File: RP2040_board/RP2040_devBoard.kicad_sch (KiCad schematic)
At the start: 27 parts, among them J1 USB_B_Micro, SW1 SW_Push, U1 RP2040, U2 AMS1117, U3 W25Q128JVS, Y1 Crystal

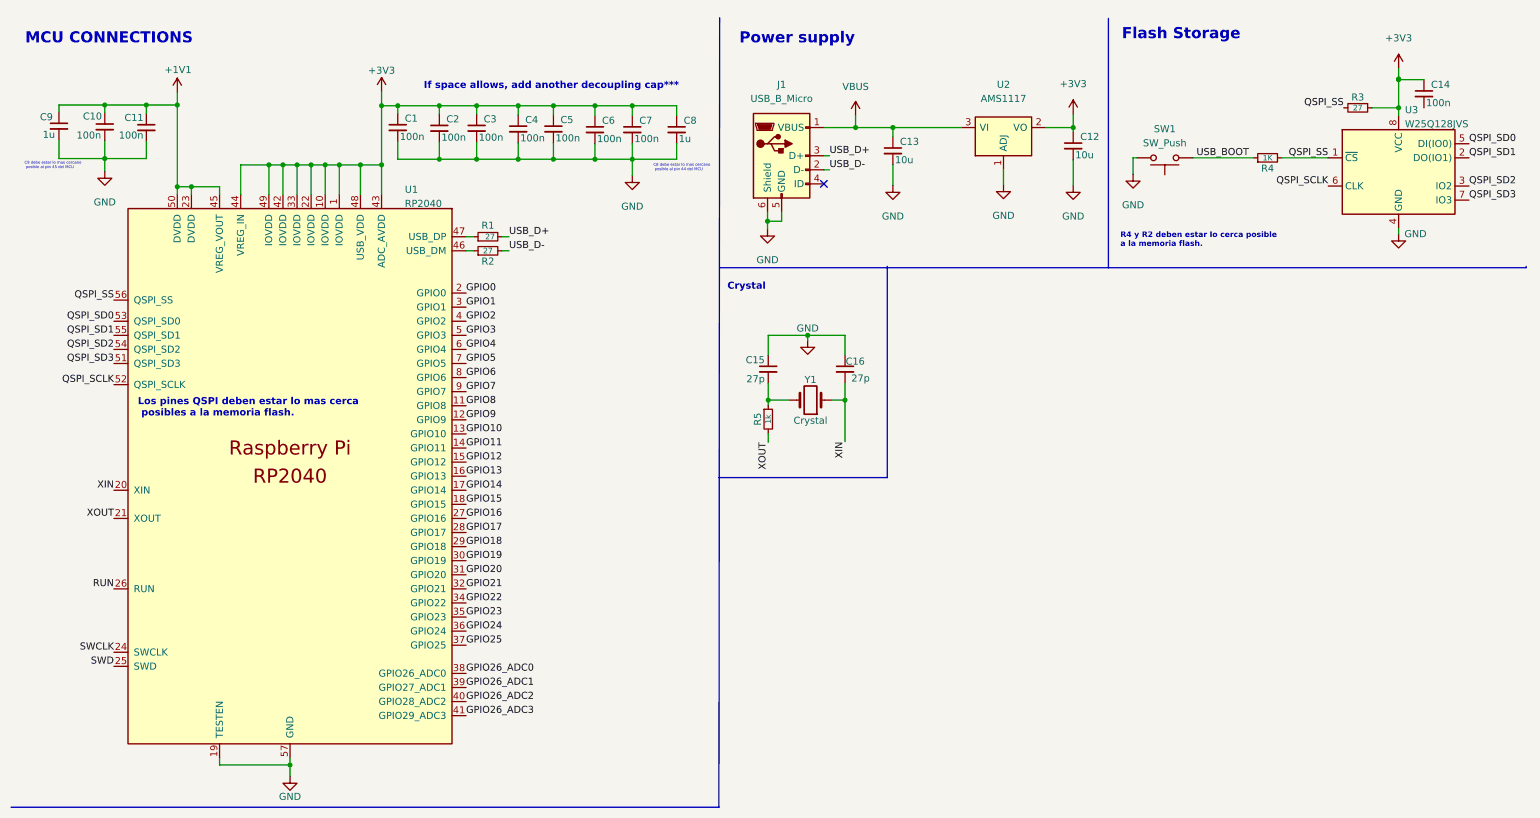
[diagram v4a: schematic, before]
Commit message: SCH: finishe with the crystal and added the pin headers
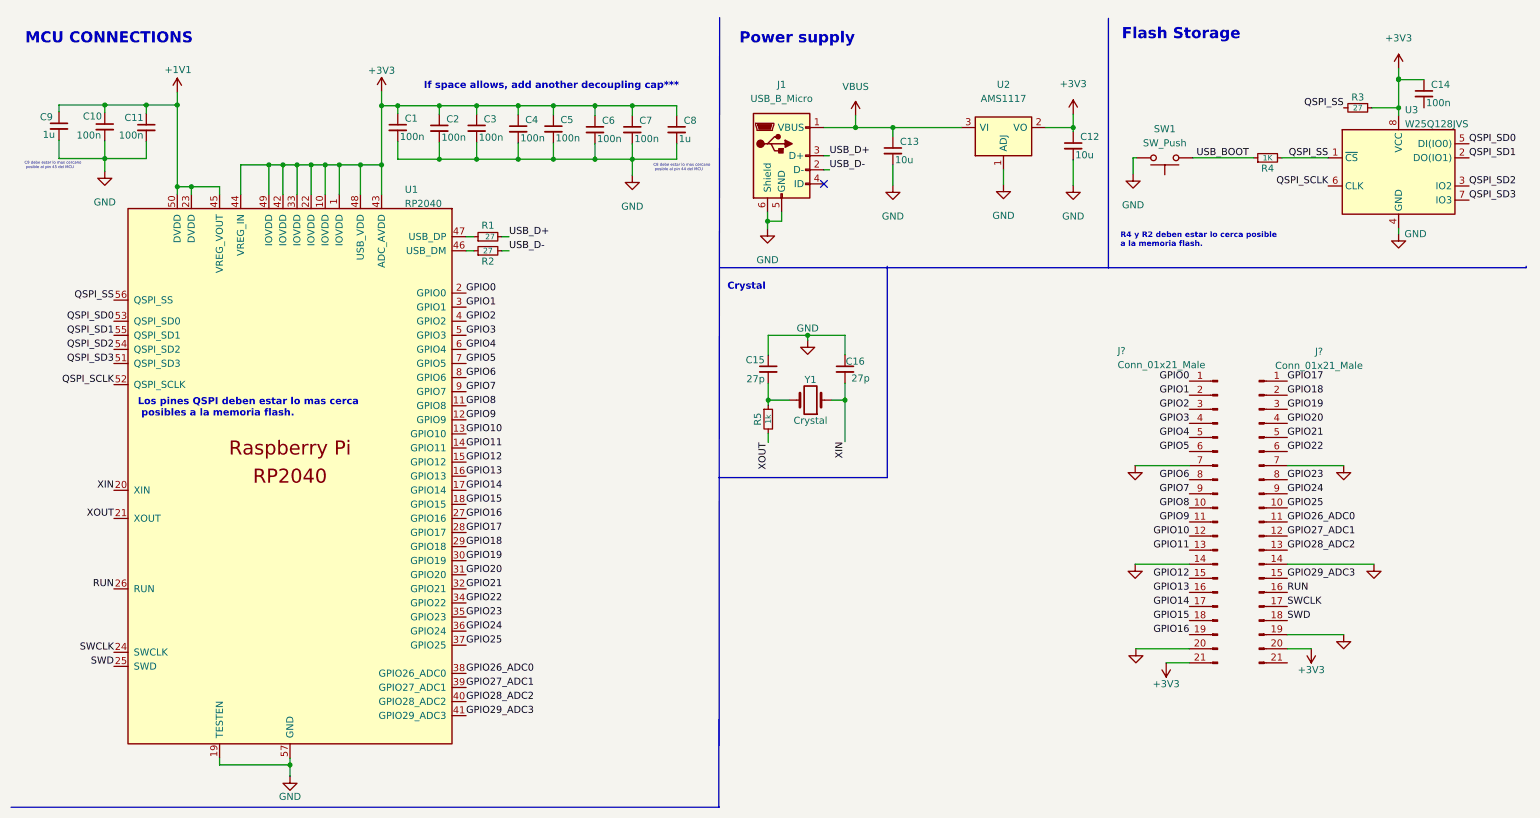
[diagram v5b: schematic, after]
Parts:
- added J? (x2): Conn_01x21_Male, symbol Connector:Conn_01x21_Male
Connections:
- net +3V3: now also J?.20 (Pin_20), J?.21 (Pin_21)
- net GND: now also J?.14 (Pin_14), J?.14 (Pin_14), J?.19 (Pin_19), J?.20 (Pin_20), J?.7 (Pin_7), J?.7 (Pin_7)
- net GPIO0: now also J?.1 (Pin_1)
- net GPIO1: now also J?.2 (Pin_2)
- net GPIO10: now also J?.12 (Pin_12)
- net GPIO11: now also J?.13 (Pin_13)
- net GPIO12: now also J?.15 (Pin_15)
- net GPIO13: now also J?.16 (Pin_16)
- net GPIO14: now also J?.17 (Pin_17)
- net GPIO15: now also J?.18 (Pin_18)
- net GPIO16: now also J?.19 (Pin_19)
- net GPIO17: now also J?.1 (Pin_1)
- net GPIO18: now also J?.2 (Pin_2)
- net GPIO19: now also J?.3 (Pin_3)
- net GPIO2: now also J?.3 (Pin_3)
- net GPIO20: now also J?.4 (Pin_4)
- net GPIO21: now also J?.5 (Pin_5)
- net GPIO22: now also J?.6 (Pin_6)
- net GPIO23: now also J?.8 (Pin_8)
- net GPIO24: now also J?.9 (Pin_9)
- net GPIO25: now also J?.10 (Pin_10)
- net GPIO26_ADC0: now also J?.11 (Pin_11)
- net GPIO3: now also J?.4 (Pin_4)
- net GPIO4: now also J?.5 (Pin_5)
- net GPIO5: now also J?.6 (Pin_6)
- net GPIO6: now also J?.8 (Pin_8)
- net GPIO7: now also J?.9 (Pin_9)
- net GPIO8: now also J?.10 (Pin_10)
- net GPIO9: now also J?.11 (Pin_11)
- net RUN: now also J?.16 (Pin_16)
- net SWCLK: now also J?.17 (Pin_17)
- net SWD: now also J?.18 (Pin_18)
- net GPIO26_ADC1 renamed GPIO27_ADC1
- net GPIO27_ADC1: now also J?.12 (Pin_12)
- net GPIO26_ADC2 renamed GPIO28_ADC2
- net GPIO28_ADC2: now also J?.13 (Pin_13)
- net GPIO26_ADC3 renamed GPIO29_ADC3
- net GPIO29_ADC3: now also J?.15 (Pin_15)

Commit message: SCH: added 1 led for power indication and another one to the GPIO00 for testing purposes.
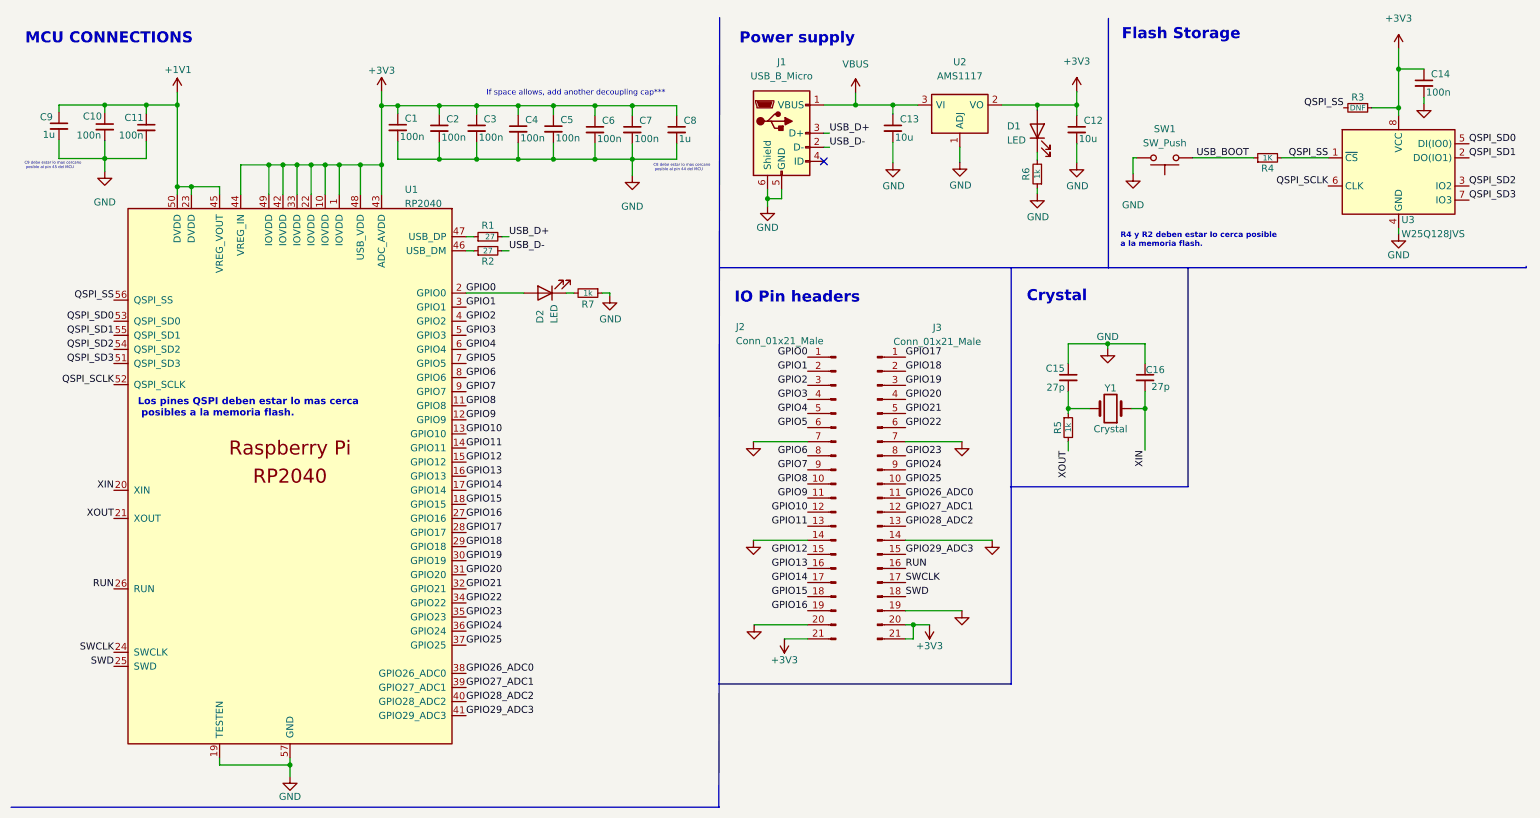
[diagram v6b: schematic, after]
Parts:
- added D1, D2: LED, symbol Device:LED
- added R6, R7: 1k, symbol Device:R_Small
- R3: value 27 -> DNF
- gave numbers to parts that had none: 2
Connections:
- net +3V3: now also C14.1, J3.21 (Pin_21), R3.1, U3.8 (VCC), D1.2 (A)
- net GND: now also C14.2, R6.1, R7.1
- net GPIO0: now also D2.2 (A)
- new net: D1.1 (K), R6.2
- new net: D2.1 (K), R7.2
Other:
- note added: "IO Pin headers"
- moved on the sheet: C12, C13, C14, C15, C16, J1, J2, J3, R5, U2, Y1
